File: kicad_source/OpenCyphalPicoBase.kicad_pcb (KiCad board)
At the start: 2 copper layers, 89 x 30 mm, 66 parts, among them CN1 RASPBERRYPI_PICO, CN10 1x04, CN11 CONN_01X03, CN12 CONN_01X03, CN13 GH_SM04B-GHS-TB, CN2 SM04B-SRSS-TB, CN3 SM04B-SRSS-TB, CN4 GH_SM04B-GHS-TB, CN5 GH_SM04B-GHS-TB, CN6 691322310002, CN7 CONN_02X03, CN8 01X08, CN9 1x04, SW1 SPST, U3 24LC64, U4 MCP2515, U8 MCP2515, U9 SN65HVD232, Y1 16MHz, Y2 16MHz

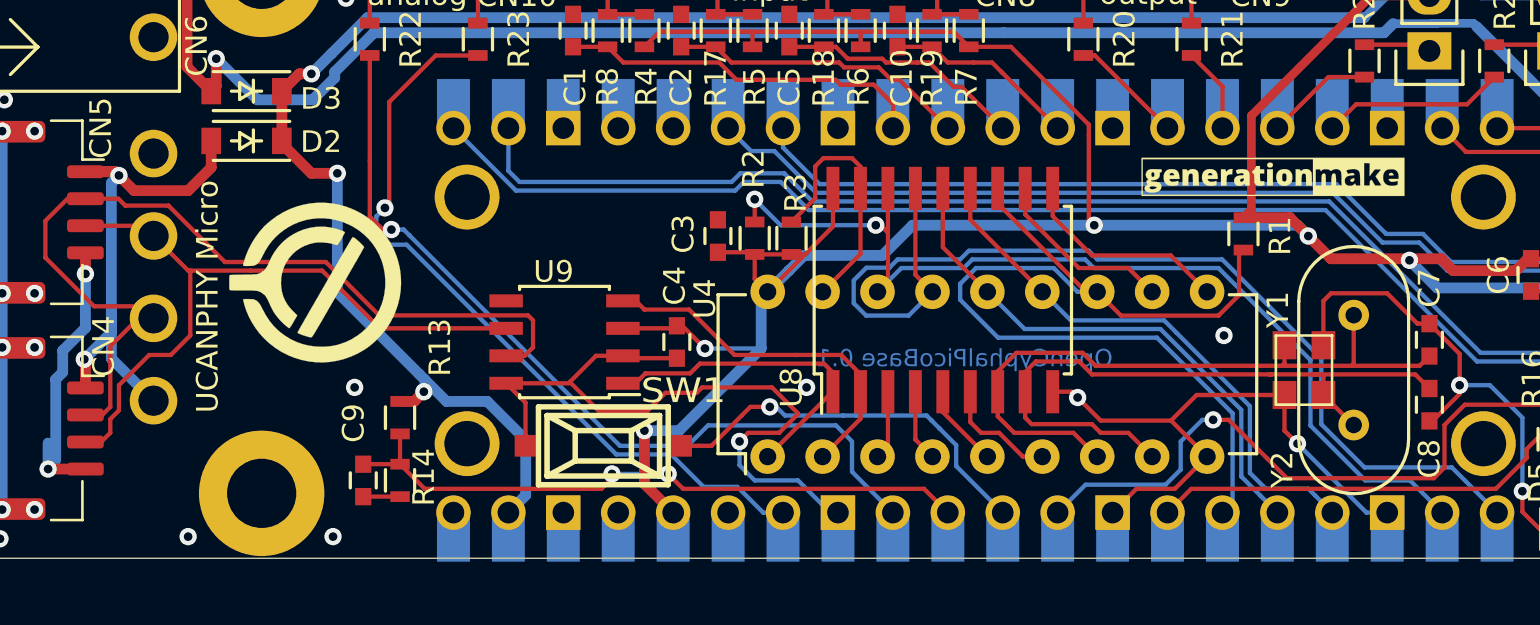
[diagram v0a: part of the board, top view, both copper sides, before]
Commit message: saved project with kicad 6
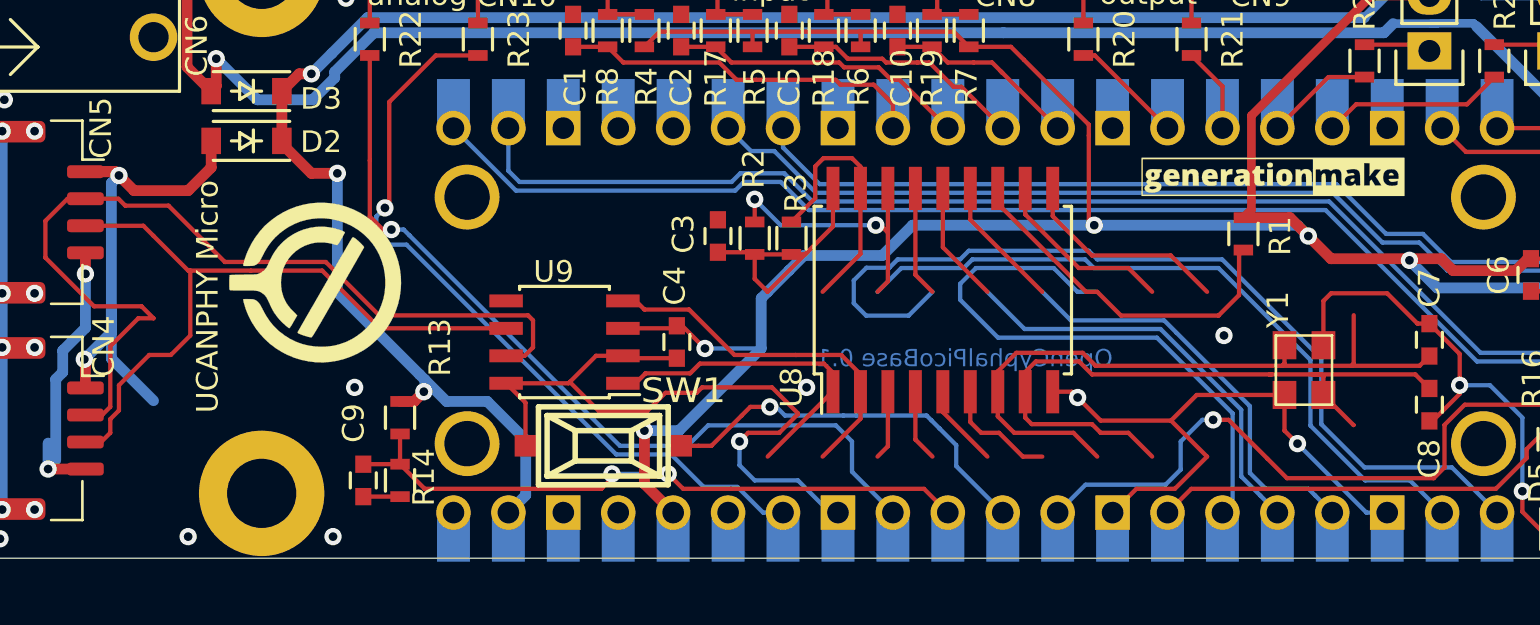
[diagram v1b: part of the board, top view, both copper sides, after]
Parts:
- removed CN13: GH_SM04B-GHS-TB, CON_wuerth:WR-TBL_691322310004
- removed U4: MCP2515, DIP:DIP-18_W7.62mm
- removed Y2: 16MHz, crystals:HC-49V
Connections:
- CN1 pad 35: Net-(CN1-Pad35) -> unconnected-(CN1-Pad35)
- CN1 pad 37: Net-(CN1-Pad37) -> unconnected-(CN1-Pad37)
- CN1 pad 4: Net-(CN1-Pad4) -> unconnected-(CN1-Pad4)
- CN1 pad 40: Net-(CN1-Pad40) -> unconnected-(CN1-Pad40)
- CN1 pad 5: Net-(CN1-Pad5) -> unconnected-(CN1-Pad5)
- MECH1 pad 1: (no net) -> unconnected-(MECH1-Pad1)
- MECH2 pad 1: (no net) -> unconnected-(MECH2-Pad1)
- MECH3 pad 1: (no net) -> unconnected-(MECH3-Pad1)
- MECH4 pad 1: (no net) -> unconnected-(MECH4-Pad1)
- U9 pad 5: (no net) -> unconnected-(U9-Pad5)
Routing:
- net unconnected-(CN1-Pad5): track 0.00 -> 1.27 mm
- net unconnected-(CN1-Pad40): track 0.00 -> 1.27 mm
- net unconnected-(CN1-Pad4): track 0.00 -> 1.27 mm
- net unconnected-(CN1-Pad37): track 0.00 -> 1.27 mm
- net unconnected-(CN1-Pad35): track 0.00 -> 1.27 mm
- net Net-(CN1-Pad5): track 1.27 -> 0.00 mm
- net Net-(CN1-Pad40): track 1.27 -> 0.00 mm
- net Net-(CN1-Pad4): track 1.27 -> 0.00 mm
- net Net-(CN1-Pad37): track 1.27 -> 0.00 mm
- net Net-(CN1-Pad35): track 1.27 -> 0.00 mm
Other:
- net class Default removed

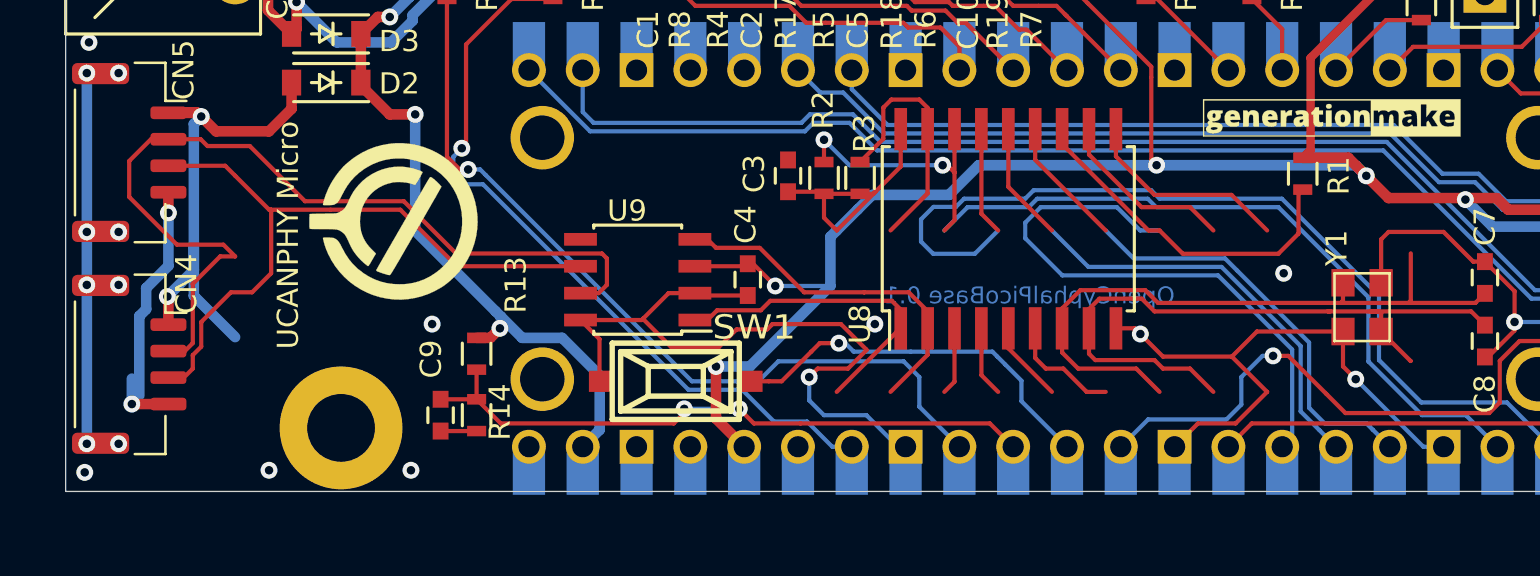
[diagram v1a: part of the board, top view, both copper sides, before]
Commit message: removed some tht parts
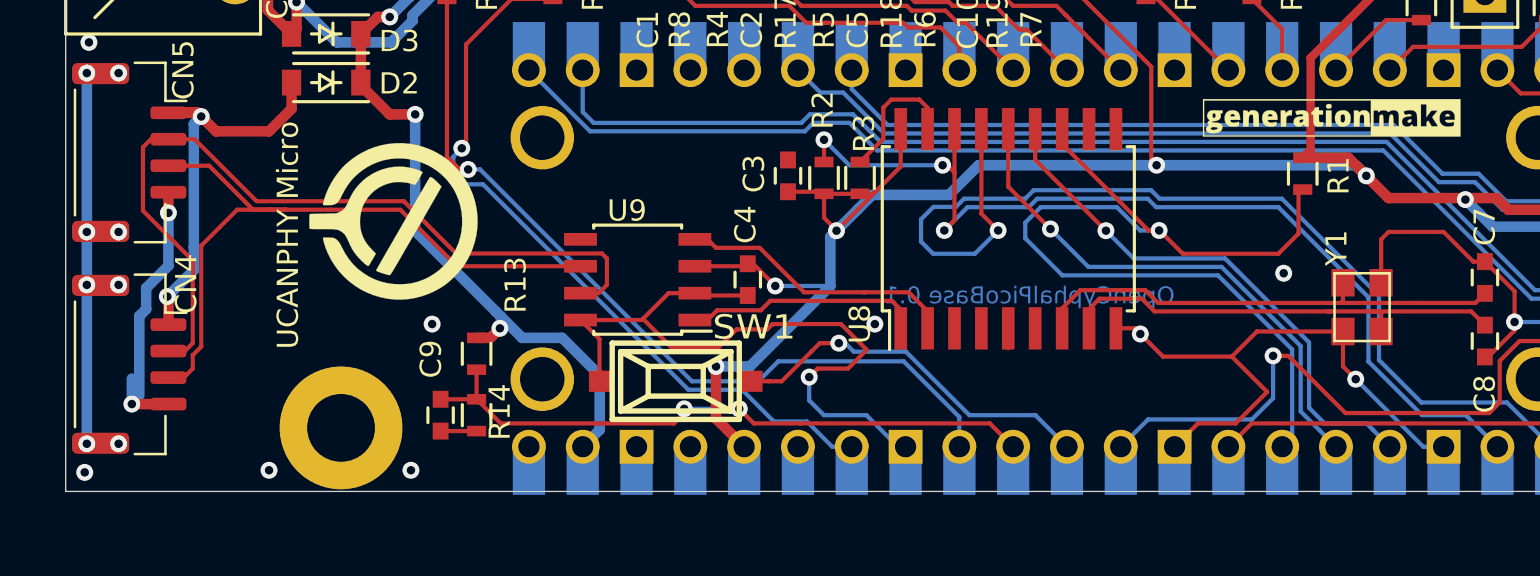
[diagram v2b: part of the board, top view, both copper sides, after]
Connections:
- net /RESERVED1 renamed /NEOPIXEL
- net /RESERVED1_R renamed /NEOPIXEL_R
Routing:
- net /MCP2515/MCP2515_RX1BUF: track 9.87 -> 0.00 mm
- net /MCP2515/MCP2515_OSC1: track 31.6 -> 21.8 mm
- net /MCP2515/MCP2515_OSC2: track 31.4 -> 22.7 mm
- net /MCP2515/MCP2515_RX0BUF: track 8.55 -> 0.00 mm
- net /MCP2515/MCP2515_RESET: track 11.9 -> 6.44 mm
- net /MCP2515/MCP2515_TX2RTS: track 5.19 -> 0.00 mm
- net /MCP2515/CANVCC: track 24.8 -> 19.8 mm
- net /MCP2515/TXCAN: track 15.3 -> 11.1 mm
- net /MCP2515/CANH: track 42.5 -> 38.6 mm
- net /MCP2515/RXCAN: track 16.7 -> 13.2 mm
- net /MCP2515/MCP2515_TX0RTS: track 3.13 -> 0.00 mm
- net /MCP2515/MCP2515_SOF: track 3.00 -> 0.00 mm
- net /MCP2515/MCP2515_TX1RTS: track 3.65 -> 0.74 mm
- net /MCP2515/CANL: track 32.4 -> 33.5 mm
- net /RESET: track 19.5 -> 18.9 mm
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
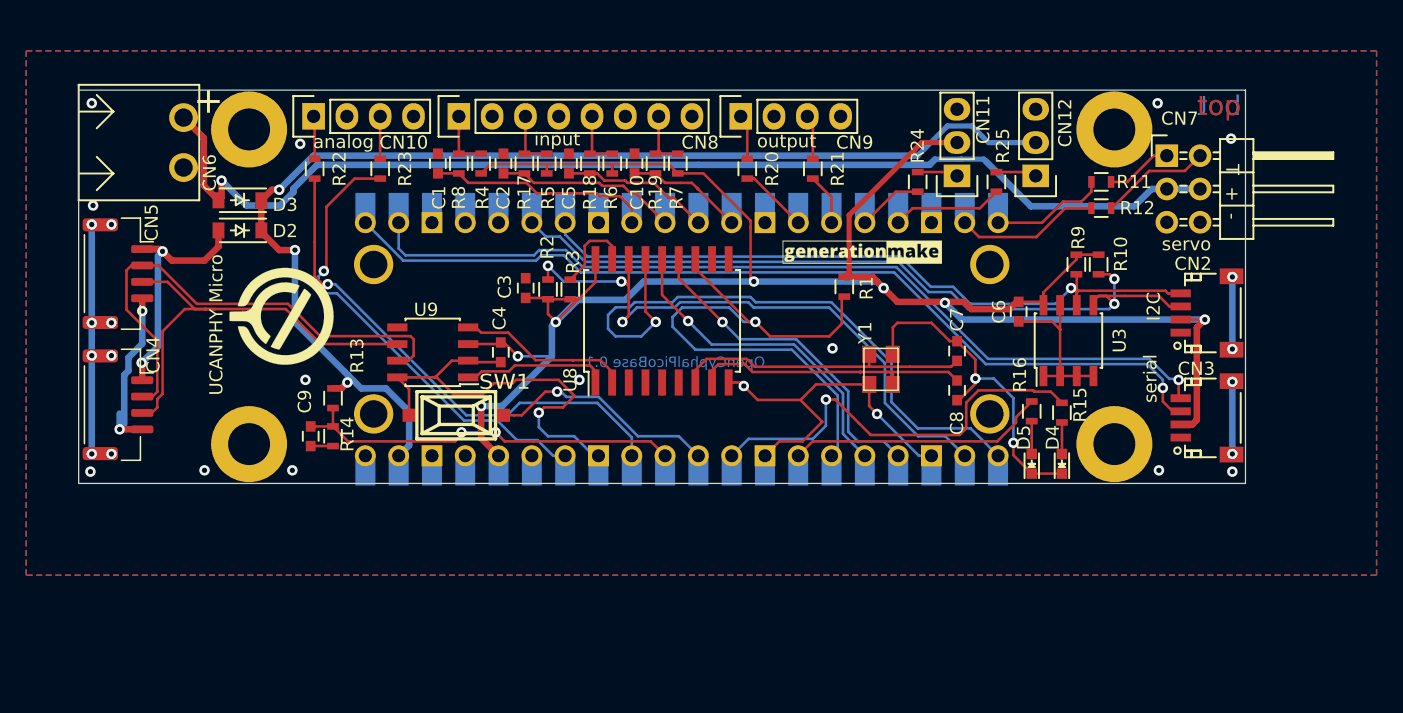
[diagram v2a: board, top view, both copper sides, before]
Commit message: switched Raspberry Pi Pico to direct solder only
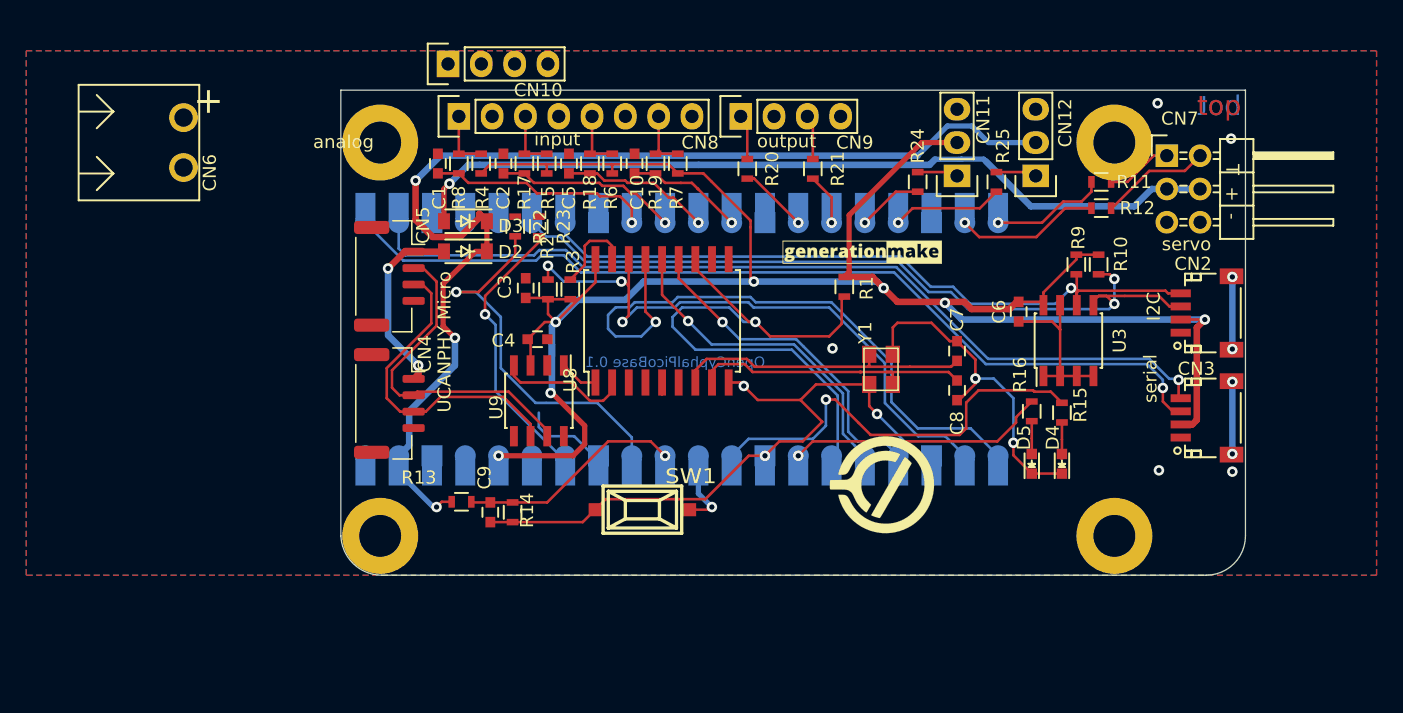
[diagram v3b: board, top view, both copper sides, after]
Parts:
- CN1: footprint MODULE_compute:RASPI_PICO_SOLDER -> generationmake:RASPI_PICO_SOLDER_Kopie
- moved L3 47.6 mm to (105.3, 103.1)
- moved L2 31.1 mm to (79.6, 108.6), turned to 180 degrees
- moved CN5 20.7 mm to (67.7, 87.2)
- moved CN4 20.7 mm to (67.7, 96.9)
- moved D2 17.3 mm to (73.5, 85.3)
- moved D3 17.3 mm to (73.5, 83.0)
- moved SW1 15.9 mm to (87.0, 105.0)
- moved R22 15.9 mm to (77.3, 83.4)
- moved C9 14.9 mm to (75.4, 105.2)
- moved R14 14.9 mm to (77.1, 105.2)
- moved R23 12.9 mm to (79.1, 83.4)
- moved R13 12.6 mm to (73.2, 104.4), turned to 0 degrees
- moved MECH3 12.2 mm to (67.0, 107.0)
- moved CN10 11.0 mm to (72.2, 71.0)
- moved MECH1 10.0 mm to (67.0, 77.0)
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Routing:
- net /V_IN: track 88.1 -> 63.1 mm
- net (no net): track 34.5 -> 11.0 mm, vias 12 -> 4
- net GND: track 115.4 -> 96.6 mm, vias 20 -> 10
- net /ANALOG_INPUT1: track 36.8 -> 22.5 mm
- net /MCP2515/CANH: track 38.6 -> 25.5 mm
- net /+BATT_MEAS: track 31.3 -> 18.5 mm, vias 2 -> 1
- net /RESET: track 18.9 -> 6.12 mm
- net /ANALOG_INPUT0: track 40.3 -> 30.0 mm
- net /MCP2515/CANL: track 33.5 -> 24.7 mm
- net /MCP2515/TXCAN: track 11.1 -> 2.95 mm
- net /MCP2515/CANVCC: track 19.8 -> 14.3 mm
- net /ANALOG_INPUT0_R: track 3.28 -> 0.00 mm
- net /ANALOG_INPUT1_R: track 3.25 -> 0.00 mm
- net +BATT: track 92.3 -> 89.1 mm
- net /MCP2515/RXCAN: track 13.2 -> 10.1 mm
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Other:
- board size 89 x 30 mm -> 69 x 37 mm
- board text removed: "CANVCC | CANH | CANL | GND"

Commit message: reworked library references
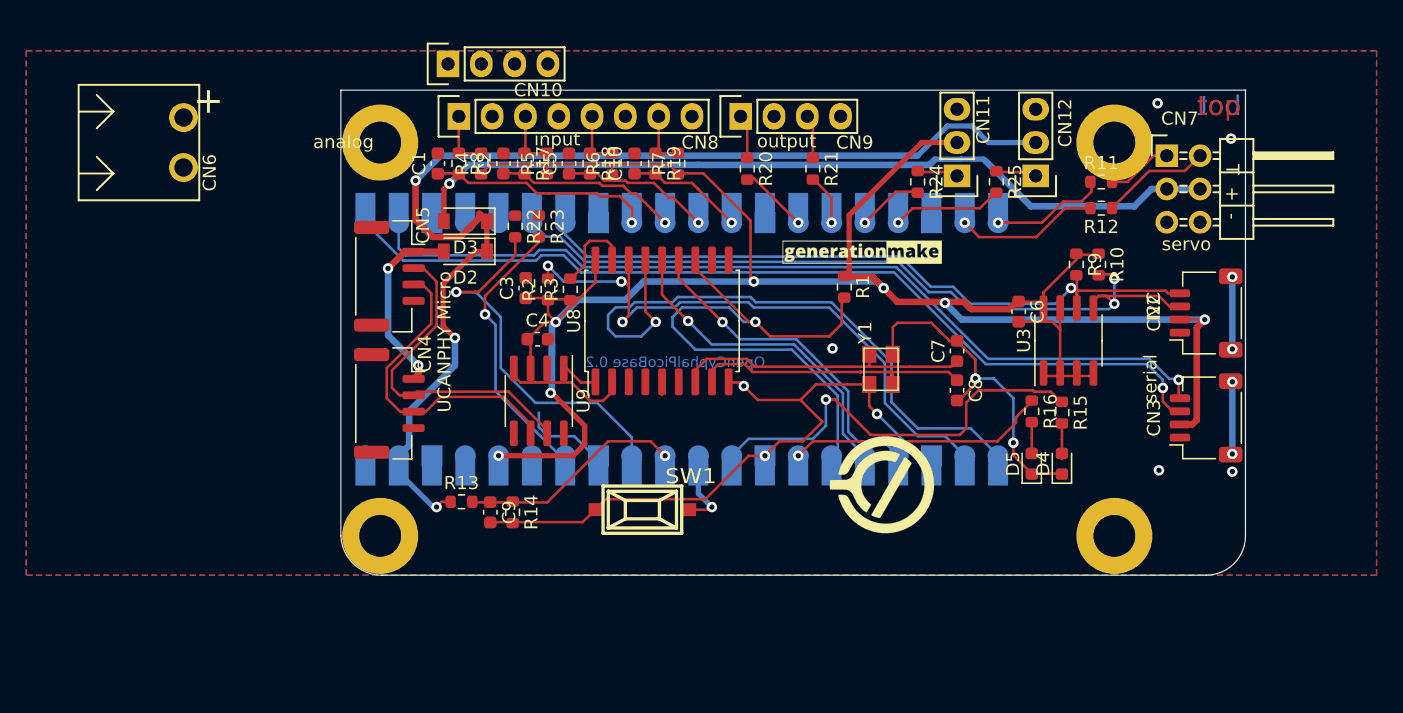
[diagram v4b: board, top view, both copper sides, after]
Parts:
- C1, C10, C2, C3, C4, C5, C6, C7, C8, C9: footprint capacitors:C_0603 -> Capacitor_SMD:C_0603_1608Metric
- CN2, CN3: footprint connectors_JST_SH:Connectors_JST_SM04B-SRSS-TB -> Connector_JST:JST_SH_SM04B-SRSS-TB_1x04-1MP_P1.00mm_Horizontal
- D2, D3: footprint diodes:SOD-123 -> Diode_SMD:D_SOD-123
- D4, D5: footprint LEDs:LED_0603 -> LED_SMD:LED_0603_1608Metric
- R1, R10, R11, R12, R13, R14, R15, R16, R17, R18, R19, R2, R20, R21, R22, R23, R24, R25, R3, R4, R5, R6, R7, R8, R9: footprint resistors:R_0603 -> Resistor_SMD:R_0603_1608Metric
- U3, U9: footprint SOIC:SOIC-8_3.9x4.9mm_Pitch1.27mm -> Package_SO:SOIC-8_3.9x4.9mm_P1.27mm
- U8: footprint SOIC:SOIC-18_7.5x11.6mm_Pitch1.27mm -> Package_SO:SOIC-18W_7.5x11.6mm_P1.27mm
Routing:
- net +3V3: track 162.1 -> 187.5 mm, vias 7 -> 8
- net /INPUT2: track 12.7 -> 0.00 mm, vias 1 -> 0
- net GND: track 96.6 -> 84.0 mm
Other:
- board text added: "OpenCyphalPicoBase 0.2"
- board text removed: "OpenCyphalPicoBase 0.1"
